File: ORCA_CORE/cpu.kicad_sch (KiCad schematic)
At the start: 47 parts, among them J10 Raspberry_Pi_2_3, J11 I2C, J12 I2C, J13 6Vout, J15 Conn_01x05_Pin, J16 Conn_01x05_Pin, J20 5Vout, P1 USB_C_Plug_USB2.0, Q6 BSS138, Q7 BSS138, Q8 BSS138, U13 FT230XS, U14 BNO055, U15 NJM78055DL1

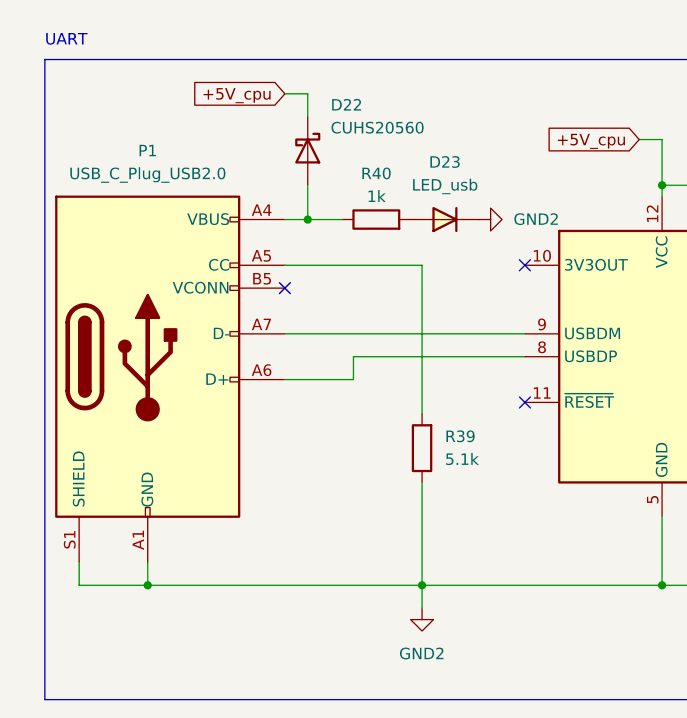
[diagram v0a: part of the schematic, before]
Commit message: wired and filled all borad
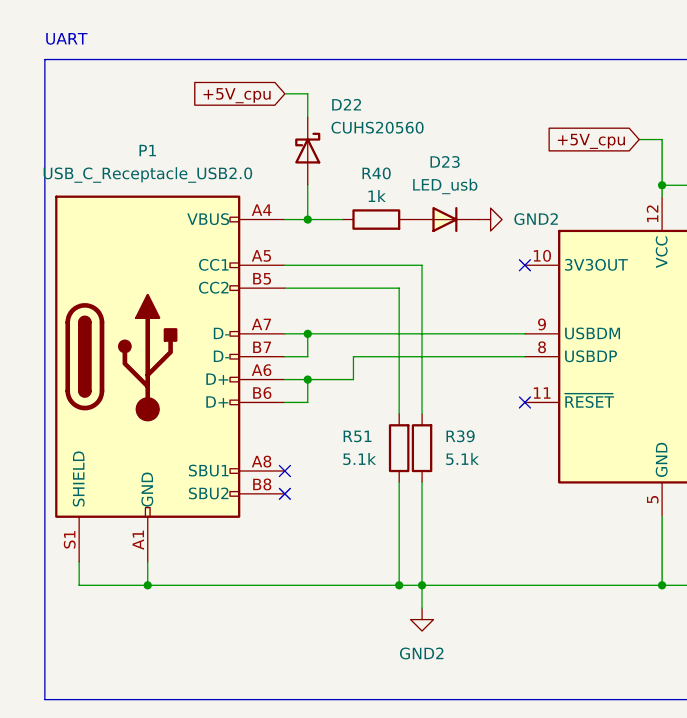
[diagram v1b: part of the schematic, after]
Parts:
- removed P1: USB_C_Plug_USB2.0, Connector_USB:USB_C_Receptacle_HCTL_HC-TYPE-C-16P-01A_withmodel, symbol Connector:USB_C_Plug_USB2.0
- added P1: USB_C_Receptacle_USB2.0, Conn:USB_C_Receptacle_XKB_U262-16XN-4BVC11, symbol Connector:USB_C_Receptacle_USB2.0
- added R51: 5.1k, Resistor_SMD:R_0603_1608Metric_Pad0.98x0.95mm_HandSolder, symbol Device:R
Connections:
- net GND2: now also P1.A1 (GND), P1.A12 (GND), P1.B1 (GND), P1.B12 (GND), P1.S1 (SHIELD), R51.1
- net at D22.2 (A), R40.1: now also P1.A4 (VBUS), P1.A9 (VBUS), P1.B4 (VBUS), P1.B9 (VBUS)
- net at R39.2: now also P1.A5 (CC1)
- net at U13.8 (USBDP): now also P1.A6 (D+), P1.B6 (D+)
- net at U13.9 (USBDM): now also P1.A7 (D-), P1.B7 (D-)
- new net: P1.B5 (CC2), R51.2
- no-connect marks 23 -> 24
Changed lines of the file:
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@@
   (junction (at 132.08 83.82) (diameter 0) (color 0 0 0 0)
   )
+  (junction (at 54.61 171.45) (diameter 0) (color 0 0 0 0)
+  )
   (junction (at 41.91 82.55) (diameter 0) (color 0 0 0 0)
   )
@@
   (junction (at 177.8 30.48) (diameter 0) (color 0 0 0 0)
   )
+  (junction (at 44.45 148.59) (diameter 0) (color 0 0 0 0)
+  )
   (junction (at 132.08 72.39) (diameter 0) (color 0 0 0 0)
   )
@@
   (junction (at 182.88 97.79) (diameter 0) (color 0 0 0 0)
   )
+  (junction (at 44.45 143.51) (diameter 0) (color 0 0 0 0)
+  )
   (junction (at 180.34 97.79) (diameter 0) (color 0 0 0 0)
   )
@@
   )
   (no_connect (at 104.14 143.51))
-  (no_connect (at 41.91 138.43))
   (no_connect (at 273.05 33.02))
   (no_connect (at 104.14 153.67))
@@
   (no_connect (at 203.2 44.45))
   (no_connect (at 68.58 151.13))
+  (no_connect (at 41.91 158.75))
   (no_connect (at 203.2 67.31))
   (no_connect (at 203.2 62.23))
   (no_connect (at 68.58 135.89))
+  (no_connect (at 41.91 161.29))
   (no_connect (at 203.2 74.93))
   (no_connect (at 203.2 59.69))
@@
     (stroke (width 0) (type default))
   )
-  (wire (pts (xy 41.91 148.59) (xy 49.53 148.59))
+  (wire (pts (xy 41.91 148.59) (xy 44.45 148.59))
     (stroke (width 0) (type default))
   )
@@
     (stroke (width 0) (type default))
   )
+  (wire (pts (xy 44.45 151.13) (xy 44.45 148.59))
+    (stroke (width 0) (type default))
+  )
   (wire (pts (xy 36.83 21.59) (xy 45.72 21.59))
     (stroke (width 0) (type default))
@@
     (stroke (width 0) (type default))
   )
-  (wire (pts (xy 41.91 143.51) (xy 68.58 143.51))
+  (wire (pts (xy 41.91 143.51) (xy 44.45 143.51))
     (stroke (width 0) (type default))
   )
@@
     (stroke (width 0) (type default))
   )
+  (wire (pts (xy 41.91 151.13) (xy 44.45 151.13))
+    (stroke (width 0) (type default))
+  )
   (wire (pts (xy 57.15 171.45) (xy 57.15 173.99))
     (stroke (width 0) (type default))
@@
     (stroke (width 0) (type default))
   )
+  (wire (pts (xy 41.91 146.05) (xy 44.45 146.05))
+    (stroke (width 0) (type default))
+  )
   (wire (pts (xy 25.4 35.56) (xy 27.94 35.56))
     (stroke (width 0) (type default))
@@
     (stroke (width 0) (type default))
   )
+  (wire (pts (xy 54.61 160.02) (xy 54.61 171.45))
+    (stroke (width 0) (type default))
+  )
   (wire (pts (xy 44.45 130.81) (xy 48.26 130.81))
     (stroke (width 0) (type default))
@@
     (stroke (width 0) (type default))
   )
-  (wire (pts (xy 26.67 171.45) (xy 57.15 171.45))
+  (wire (pts (xy 26.67 171.45) (xy 54.61 171.45))
     (stroke (width 0) (type default))
   )
@@
     (stroke (width 0) (type default))
   )
+  (wire (pts (xy 44.45 146.05) (xy 44.45 143.51))
+    (stroke (width 0) (type default))
+  )
   (wire (pts (xy 107.95 19.05) (xy 107.95 22.86))
     (stroke (width 0) (type default))
@@
     (stroke (width 0) (type default))
   )
+  (wire (pts (xy 54.61 138.43) (xy 54.61 152.4))
+    (stroke (width 0) (type default))
+  )
   (wire (pts (xy 83.82 171.45) (xy 57.15 171.45))
     (stroke (width 0) (type default))
@@
     (stroke (width 0) (type default))
   )
+  (wire (pts (xy 44.45 143.51) (xy 68.58 143.51))
+    (stroke (width 0) (type default))
+  )
   (wire (pts (xy 203.2 82.55) (xy 210.82 82.55))
     (stroke (width 0) (type default))
@@
     (stroke (width 0) (type default))
   )
+  (wire (pts (xy 44.45 148.59) (xy 49.53 148.59))
+    (stroke (width 0) (type default))
+  )
   (wire (pts (xy 158.75 129.54) (xy 166.37 129.54))
     (stroke (width 0) (type default))
@@
     (stroke (width 0) (type default))
   )
+  (wire (pts (xy 41.91 138.43) (xy 54.61 138.43))
+    (stroke (width 0) (type default))
+  )
   (wire (pts (xy 45.72 29.21) (xy 54.61 29.21))
+    (stroke (width 0) (type default))
+  )
+  (wire (pts (xy 54.61 171.45) (xy 57.15 171.45))
     (stroke (width 0) (type default))
   )
@@
         (path "/895d6bb7-4008-488b-a34b-0077e9f7e4a1/e25f2ef8-8e13-4e8d-9b3a-975318177c66"
           (reference "R40") (unit 1)
+        )
+      )
+    )
+  )
+  (symbol (lib_id "Connector:USB_C_Receptacle_USB2.0") (at 26.67 146.05 0) (unit 1)
+    (in_bom yes) (on_board yes) (dnp no) (fields_autoplaced)
+    (property "Reference" "P1" (at 26.67 123.19 0)
+      (effects (font (size 1.27 1.27)))
+    )
+    (property "Value" "USB_C_Receptacle_USB2.0" (at 26.67 125.73 0)
+      (effects (font (size 1.27 1.27)))
+    )
+    (property "Footprint" "Conn:USB_C_Receptacle_XKB_U262-16XN-4BVC11" (at 30.48 146.05 0)
+      (effects (font (size 1.27 1.27)) hide)
+    )
+    (property "Datasheet" "https://www.usb.org/sites/default/files/documents/usb_type-c.zip" (at 30.48 146.05 0)
+      (effects (font (size 1.27 1.27)) hide)
+    )
+    (pin "A1")
+    (pin "A12")
+    (pin "A4")
+    (pin "A5")
+    (pin "A6")
+    (pin "A7")
+    (pin "A8")
+    (pin "A9")
+    (pin "B1")
+    (pin "B12")
+    (pin "B4")
+    (pin "B5")
+    (pin "B6")
+    (pin "B7")
+    (pin "B8")
+    (pin "B9")
+    (pin "S1")
+    (instances
+      (project "ORCA_CORE"
+        (path "/895d6bb7-4008-488b-a34b-0077e9f7e4a1/e25f2ef8-8e13-4e8d-9b3a-975318177c66"
+          (reference "P1") (unit 1)
+        )
+      )
+    )
+  )
+  (symbol (lib_id "Device:R") (at 54.61 156.21 180) (unit 1)
+    (in_bom yes) (on_board yes) (dnp no)
+    (property "Reference" "R51" (at 48.26 154.94 0)
+      (effects (font (size 1.27 1.27)) (justify right))
+    )
+    (property "Value" "5.1k" (at 48.26 157.48 0)
+      (effects (font (size 1.27 1.27)) (justify right))
+    )
+    (property "Footprint" "Resistor_SMD:R_0603_1608Metric_Pad0.98x0.95mm_HandSolder" (at 56.388 156.21 90)
+      (effects (font (size 1.27 1.27)) hide)
+    )
+    (property "Datasheet" "~" (at 54.61 156.21 0)
+      (effects (font (size 1.27 1.27)) hide)
+    )
+    (pin "2")
+    (pin "1")
+    (instances
+      (project "ORCA_CORE"
+        (path "/895d6bb7-4008-488b-a34b-0077e9f7e4a1/e25f2ef8-8e13-4e8d-9b3a-975318177c66"
+          (reference "R51") (unit 1)
         )
       )
@@
         )
       )
-    )
-  )
-  (symbol (lib_id "Connector:USB_C_Plug_USB2.0") (at 26.67 146.05 0) (unit 1)
-    (in_bom yes) (on_board yes) (dnp no) (fields_autoplaced)
-    (property "Reference" "P1" (at 26.67 123.19 0)
-      (effects (font (size 1.27 1.27)))
-    )
-    (property "Value" "USB_C_Plug_USB2.0" (at 26.67 125.73 0)
-      (effects (font (size 1.27 1.27)))
-    )
-    (property "Footprint" "Connector_USB:USB_C_Receptacle_HCTL_HC-TYPE-C-16P-01A_withmodel" (at 30.48 146.05 0)
-      (effects (font (size 1.27 1.27)) hide)
-    )
-    (property "Datasheet" "https://www.usb.org/sites/default/files/documents/usb_type-c.zip" (at 30.48 146.05 0)
-      (effects (font (size 1.27 1.27)) hide)
-    )
-    (pin "A1")
-    (pin "A12")
-    (pin "B9")
-    (pin "A6")
-    (pin "A5")
-    (pin "B5")
-    (pin "B1")
-    (pin "A9")
-    (pin "B12")
-    (pin "A7")
-    (pin "S1")
-    (pin "A4")
-    (pin "B4")
-    (instances
-      (project "ORCA_CORE"
-        (path "/895d6bb7-4008-488b-a34b-0077e9f7e4a1/e25f2ef8-8e13-4e8d-9b3a-975318177c66"
-          (reference "P1") (unit 1)
-        )
-      )

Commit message: start making ORCA_CORE
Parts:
- removed C40, C46, C47: 4.7u, Capacitor_SMD:C_0603_1608Metric_Pad1.08x0.95mm_HandSolder, symbol Device:C
- removed C44, C48: 1u, Capacitor_SMD:C_0805_2012Metric_Pad1.18x1.45mm_HandSolder, symbol Device:C
- removed C45: 0.1u, Capacitor_SMD:C_0603_1608Metric_Pad1.08x0.95mm_HandSolder, symbol Device:C
- removed C49: 1u/50V, Capacitor_SMD:C_0805_2012Metric_Pad1.18x1.45mm_HandSolder, symbol Device:C
- removed C50: 0.1u25V, Capacitor_SMD:C_0603_1608Metric_Pad1.08x0.95mm_HandSolder, symbol Device:C
- removed D20: LED_motor, LED_SMD:LED_0603_1608Metric_Pad1.05x0.95mm_HandSolder, symbol Device:LED_Filled
- removed D22, D25: CUHS20560, Diode:Diode_US2H, symbol Device:D_Schottky
- removed D23: LED_usb, LED_SMD:LED_0603_1608Metric_Pad1.05x0.95mm_HandSolder, symbol Device:D_Filled
- removed D24: WS2812B, LED_SMD:LED_WS2812B_PLCC4_5.0x5.0mm_P3.2mm, symbol LED:WS2812B
- removed J11, J12: I2C, Connector_JST:JST_XH_B3B-XH-A_1x03_P2.50mm_Vertical, symbol Connector_Generic:Conn_01x03
- removed J13: 6Vout, Conn:power_pad, symbol Connector_Generic:Conn_01x02
- removed J15, J16: Conn_01x05_Pin, Connector_PinHeader_2.54mm:PinHeader_1x05_P2.54mm_Vertical, symbol Connector:Conn_01x05_Pin
- removed J20: 5Vout, Conn:power_pad, symbol Connector_Generic:Conn_01x02
- removed P1: USB_C_Receptacle_USB2.0, Conn:USB_C_Receptacle_XKB_U262-16XN-4BVC11, symbol Connector:USB_C_Receptacle_USB2.0
- removed Q6, Q7: BSS138, Package_TO_SOT_SMD:SOT-23, symbol Transistor_FET:BSS138
- removed R36, R40: 1k, Resistor_SMD:R_0603_1608Metric_Pad0.98x0.95mm_HandSolder, symbol Device:R
- removed R39, R51: 5.1k, Resistor_SMD:R_0603_1608Metric_Pad0.98x0.95mm_HandSolder, symbol Device:R
- removed R41, R42, R43, R44, R45, R46: 2.2k, Resistor_SMD:R_0603_1608Metric_Pad0.98x0.95mm_HandSolder, symbol Device:R
- removed U13: FT230XS, Package_SO:SSOP-16_3.9x4.9mm_P0.635mm, symbol Interface_USB:FT230XS
- removed U15: NJM78055DL1, Package_TO_SOT_SMD:TO-252-2, symbol mylib:NJM7805SDL1
- added J11: wheel_left, symbol Connector:Conn_01x03_Pin
- added J8: wheel_front, symbol Connector:Conn_01x03_Pin
- added J9: wheel_right, symbol Connector:Conn_01x03_Pin
- added Q1, Q2: BSS138, Package_TO_SOT_SMD:SOT-23, symbol Transistor_FET:BSS138
- added R4, R5, R7, R8: 2.2k, Resistor_SMD:R_0603_1608Metric_Pad0.98x0.95mm_HandSolder, symbol Device:R
- added R9: 10k, symbol Device:R
- added U2: PCA9685PW_Q900_118, digikey-footprints:TSSOP-28_W4.40mm, symbol dk_PMIC-LED-Drivers:PCA9685PW_Q900_118
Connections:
- net +3V3_cpu: now also U2.28 (VDD); no longer J10.1 (3V3), J10.17 (3V3), Q8.1 (G), R37.1, R38.1, R6.1, U14.1 (VDD)
- net RXD_3V3: now also Q2.2 (S), R5.2
- net RXD_5V: now also Q2.3 (D), R8.2
- net SCL: now also U2.26 (SCL)
- net SDA: now also U2.27 (SDA)
- net TXD_3V3: now also Q1.2 (S), R4.2
- net TXD_5V: now also Q1.3 (D), R7.2
- net emerg_detector: now also R49.2; no longer R49.1
- net emerge_order: now also R48.2; no longer R48.1
- net power_checker: now also R47.2; no longer R47.1
- net +5V_cpu renamed +5V
- net +5V: now also R7.1, R8.1
- net GND2 renamed GND1
- net GND1: now also R47.1, R48.1, R49.1, J11.1 (Pin_1), J8.1 (Pin_1), J9.1 (Pin_1), R9.1, U2.14 (VSS); no longer R47.2, R48.2, R49.2
- net full_color_led_5V renamed full_color_led
- new net: R9.2, U2.1 (A0), U2.2 (A1), U2.23 (~{OE}), U2.24 (A5), U2.25 (EXTCLK), U2.3 (A2), U2.4 (A3), U2.5 (A4)
- new net +3V3: J10.1 (3V3), J10.17 (3V3), J11.2 (Pin_2), J8.2 (Pin_2), J9.2 (Pin_2), Q1.1 (G), Q2.1 (G), Q8.1 (G), R37.1, R38.1, R4.1, R5.1, R6.1, U14.1 (VDD)
- new net LED0: J8.3 (Pin_3), U2.6 (LED0)
- new net LED1: J9.3 (Pin_3), U2.7 (LED1)
- new net LED10: U2.17 (LED10)
- new net LED11: U2.18 (LED11)
- new net LED12: U2.19 (LED12)
- new net LED13: U2.20 (LED13)
- new net LED14: U2.21 (LED14)
- new net LED15: U2.22 (LED15)
- new net LED2: J11.3 (Pin_3), U2.8 (LED2)
- new net LED3: U2.9 (LED3)
- new net LED4: U2.10 (LED4)
- new net LED5: U2.11 (LED5)
- new net LED6: U2.12 (LED6)
- new net LED7: U2.13 (LED7)
- new net LED8: U2.15 (LED8)
- new net LED9: U2.16 (LED9)
- no-connect marks 24 -> 13
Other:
- note added: "under base servo"
- note removed: "DCDC 5V 1.5A"
- note removed: "out"
- moved on the sheet: D19, J10, Q8, R34, R35, R37, R38, R47, R48, R49, R6, U14

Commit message: add power registers to power_board gate driver
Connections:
- net +3V3_cpu is gone; now on net +3V3: U2.28 (VDD)
- net GPIO12 renamed limit_sw_upper_fork
- net GPIO13 renamed limit_sw_under_fork
- net GPIO16 renamed limit_sw_upper_arm
- net GPIO17 renamed limit_sw_under_arm
- net GPIO18 renamed enable_arm
- net LED10 renamed servo_3
- net LED3 renamed INA_fork
- net LED4 renamed INB_fork
- net LED5 renamed INA_arm
- net LED6 renamed INB_arm
- net LED7 renamed servo_0
- net LED8 renamed servo_1
- net LED9 renamed servo_2
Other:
- note added: "motors"
- moved on the sheet: J10, J11, J8, J9, R47, R48, R49, R9, U14, U2

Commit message: almost completed CORE
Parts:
- removed R37, R38: 2.2k, Resistor_SMD:R_0603_1608Metric_Pad0.98x0.95mm_HandSolder, symbol Device:R
- added R51, R52, R55: 100, symbol Device:R
- added R53, R54, R56: 2.2k, symbol Device:R
- added U18, U19, U20: TLP293, Package_SO:SOIC-4_4.55x2.6mm_P1.27mm, symbol Isolator:TLP293
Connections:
- net +3V3: now also R53.2, R54.2
- net GND1: now also U18.2, U19.2, U20.2
- net SCL: no longer J10.5 (SCL/GPIO3)
- net SDA: no longer J10.3 (SDA/GPIO2)
- net emerg_detector: now also R52.1; no longer J10.15 (GPIO22), R49.2
- net emerge_order: now also J10.18 (GPIO24), R47.2, R55.1, U20.3; no longer J10.16 (GPIO23), R48.2
- net power_checker: now also J10.16 (GPIO23), R48.2, R51.1, U18.3; no longer J10.18 (GPIO24), R47.2
- net GPIO19 renamed rest
- net GPIO20: no longer names the net of J10.38 (GPIO20/MOSI1)
- net GPIO21: no longer names the net of J10.40 (GPIO21/SCLK1)
- net GPIO26: no longer names the net of J10.37 (GPIO26)
- net GPIO27: no longer names the net of J10.13 (GPIO27)
- net LED11 renamed servo_camera
- net full_color_led renamed led
- new net: R52.2, U19.1
- new net: R54.1, U19.4
- new net: R51.2, U18.1
- new net: R53.1, U18.4
- new net: R55.2, U20.1
- new net: R56.1, U20.4
- new net +3V3_motor: R56.2
- new net SCL_cpu: J10.5 (SCL/GPIO3)
- new net SDA_cpu: J10.3 (SDA/GPIO2)
- new net emerge_detector: J10.15 (GPIO22), R49.2, U19.3
- no-connect marks 13 -> 17
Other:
- note added: "arm"
- note added: "camera"
- note added: "power board info"
- note removed: "I2C"
- moved on the sheet: D19, J10, J11, J8, J9, Q8, R34, R35, R47, R48, R49, R6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
